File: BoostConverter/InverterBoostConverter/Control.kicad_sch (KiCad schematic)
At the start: 49 parts, among them IC1 UCC28220D, IC2 LM358DR, IC3 UCC27424QDRQ1, Q3 SIHFR120-GE3

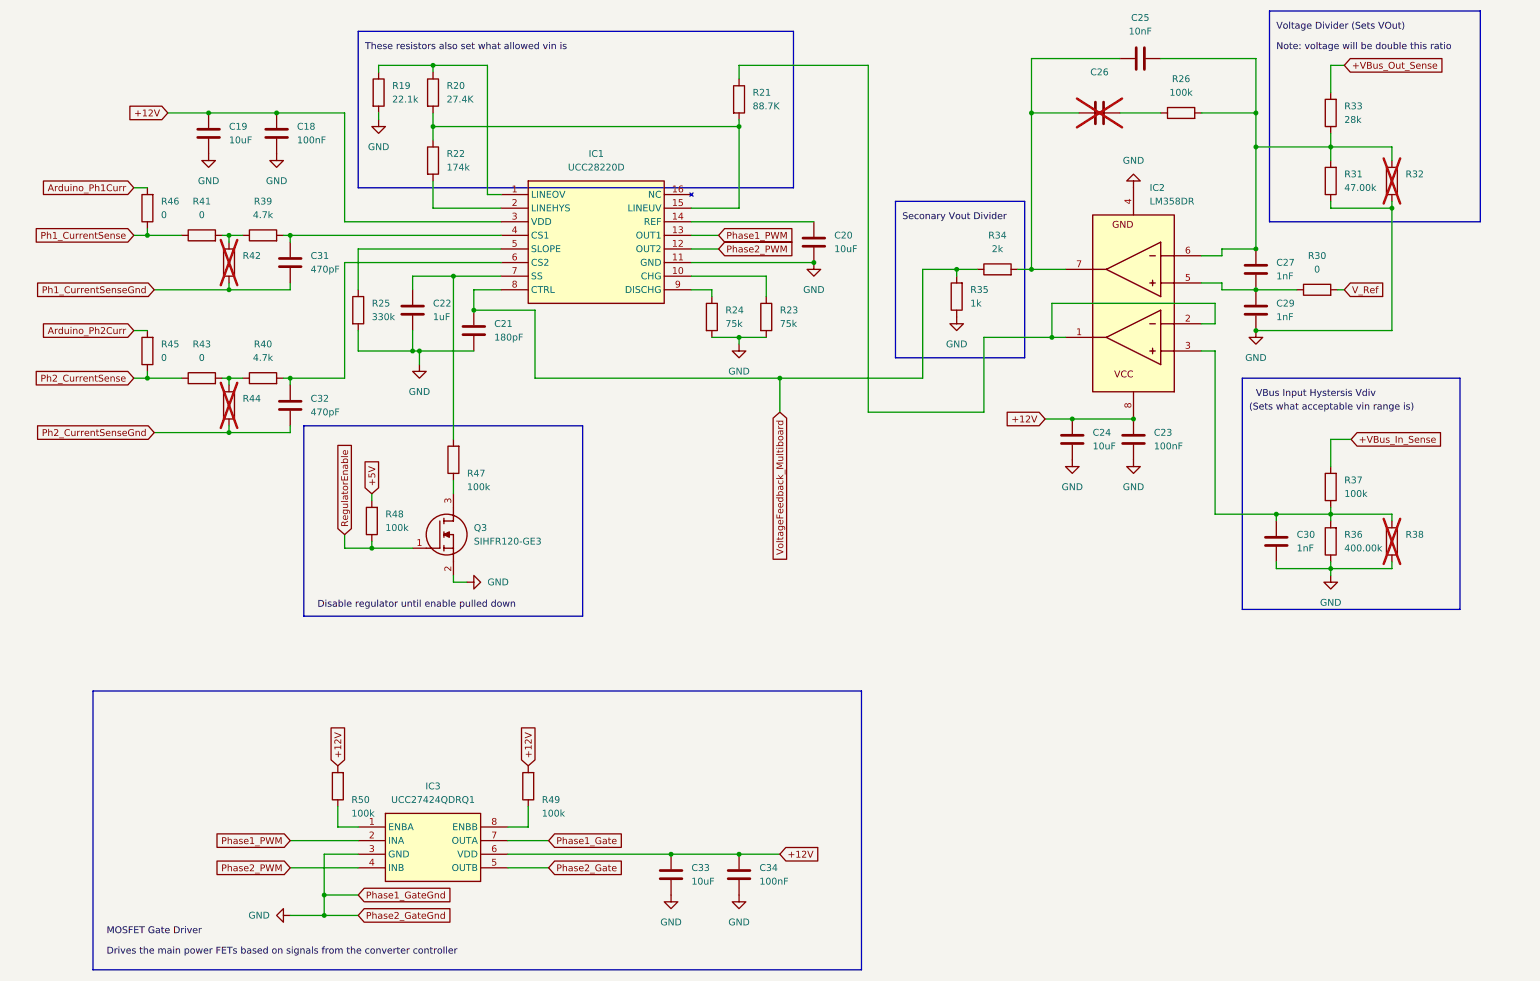
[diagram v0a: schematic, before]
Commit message: Update boost converter, add inverter
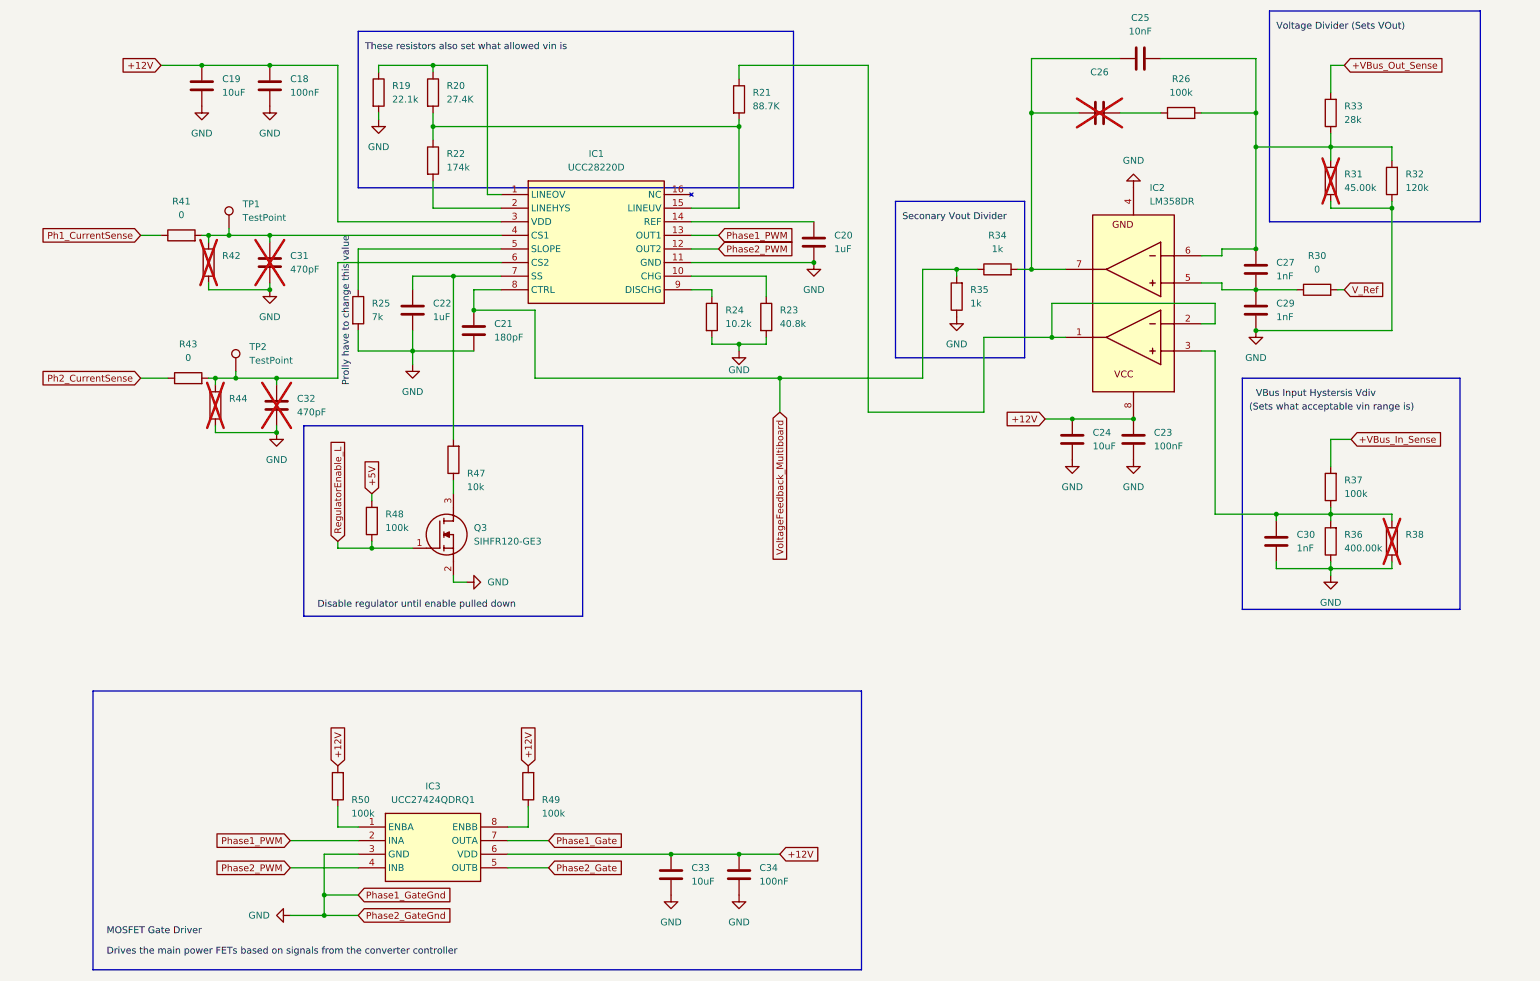
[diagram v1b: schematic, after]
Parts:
- removed R39, R40: 4.7k, 1210, symbol Device:R
- removed R45, R46: 0, 1210, symbol Device:R
- added TP1, TP2: TestPoint, symbol Connector:TestPoint
- C20: value 10uF -> 1uF
- C31, C32: now not fitted
- R23: value 75k -> 40.8k
- R24: value 75k -> 10.2k
- R25: value 330k -> 7k
- R31: value 47.00k -> 45.00k; now not fitted
- R32: value ~ -> 120k; now fitted
- R34: value 2k -> 1k
- R47: value 100k -> 10k
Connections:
- net Ph1_CurrentSenseGnd is gone; now on net GND: C31.2, R42.1
- net Ph2_CurrentSenseGnd is gone; now on net GND: C32.2, R44.1
- net at R41.2, R42.2: now also C31.1, IC1.4 (CS1), TP1.1
- net at C32.1, IC1.6 (CS2): now also R43.2, R44.2, TP2.1
- net RegulatorEnable renamed RegulatorEnable_L
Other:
- moved on the sheet: C18, C19, R41, R42, R43, R44

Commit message: Finish Boost Converter
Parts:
- added R57: 1k, Resistor_SMD:R_1210_3225Metric_Pad1.30x2.65mm_HandSolder, symbol Device:R
- added R58: 0, Resistor_SMD:R_1210_3225Metric_Pad1.30x2.65mm_HandSolder, symbol Device:R
- added R80: 100k, Resistor_SMD:R_1210_3225Metric_Pad1.30x2.65mm_HandSolder, symbol Device:R
- C18, C19, C20, C21, C22, C23, C24, C25, C26, C27, C29, C30, C31, C32, C33, C34: footprint 1210 -> Capacitor_SMD:C_1210_3225Metric_Pad1.33x2.70mm_HandSolder
- IC1: footprint UCC28220D -> InverterCom:UCC28220D
- IC2, IC3: footprint SOIC127P600X175-8N -> InverterCom:SOIC127P600X175-8N
- Q3: footprint SIHFR120GE3 -> InverterCom:SIHFR120GE3
- R19: value 22.1k -> 12.79k; footprint 1210 -> Resistor_SMD:R_1210_3225Metric_Pad1.30x2.65mm_HandSolder
- R20: value 27.4K -> 101.85k; footprint 1210 -> Resistor_SMD:R_1210_3225Metric_Pad1.30x2.65mm_HandSolder
- R21: value 88.7K -> 149.21k; footprint 1210 -> Resistor_SMD:R_1210_3225Metric_Pad1.30x2.65mm_HandSolder
- R22: value 174k -> 100k; footprint 1210 -> Resistor_SMD:R_1210_3225Metric_Pad1.30x2.65mm_HandSolder
- R23, R24, R25, R26, R30, R31, R32, R33, R34, R35, R37, R38, R41, R42, R43, R44, R47, R49, R50: footprint 1210 -> Resistor_SMD:R_1210_3225Metric_Pad1.30x2.65mm_HandSolder
- R36: value 400.00k -> 800.00k; footprint 1210 -> Resistor_SMD:R_1210_3225Metric_Pad1.30x2.65mm_HandSolder
- R48: value 100k -> 300k; footprint 1210 -> Resistor_SMD:R_1210_3225Metric_Pad1.30x2.65mm_HandSolder
- TP1, TP2: footprint (none) -> TestPoint:TestPoint_Pad_3.0x3.0mm
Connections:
- net +5V is gone; now on net +12V: R48.2
- net GND: now also R19.1, R58.2, R80.1; no longer R19.2
- net RegulatorEnable_L: now also R80.2
- net at C25.1, C26.1, IC2.7 (OUT2)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: now also R57.2
- net at C30.1, R36.2, R37.1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: now also R21.2; no longer IC2.3 (IN1+)
- net at C27.1, C29.2, IC2.5 (IN2+)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: now also IC2.3 (IN1+)
- net at C25.2, C27.2, IC2.6 (IN2-)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: now also IC2.2 (IN1-)
- net at IC1.1 (LINEOV), R20.1: now also R19.2; no longer R19.1
- net at IC1.15 (LINEUV), R20.2: now also R21.1, R22.2; no longer R21.2, R22.1
- net at IC1.2 (LINEHYS): now also R22.1; no longer R22.2
- new net: IC2.1 (OUT1), R57.1
- new net GNDPWR: R58.1
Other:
- moved on the sheet: C18, C19, R19, R20, R21, R22, R37
